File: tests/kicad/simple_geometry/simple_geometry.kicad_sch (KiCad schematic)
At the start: 2 parts

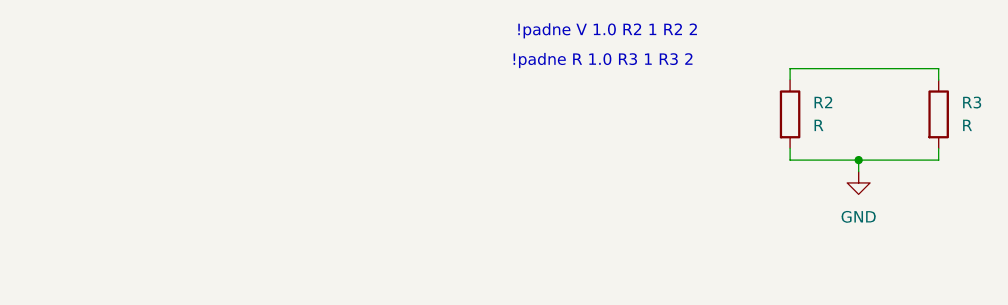
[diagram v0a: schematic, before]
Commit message: kicad: Implement basic eeschema directive parsing
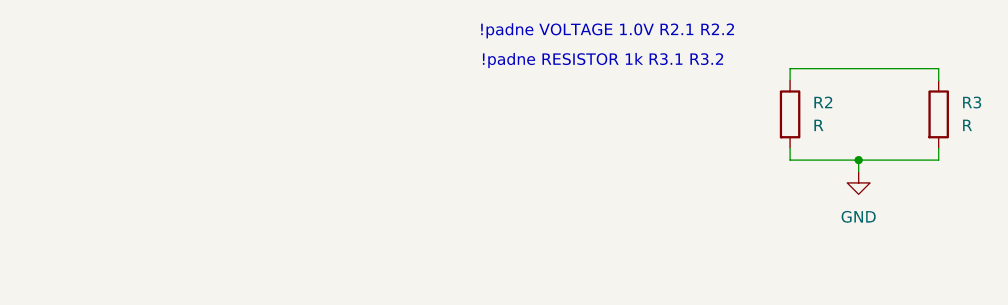
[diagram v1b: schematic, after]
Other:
- note added: "!padne RESISTOR 1k R3.1 R3.2"
- note added: "!padne VOLTAGE 1.0V R2.1 R2.2"
- note removed: "!padne R 1.0 R3 1 R3 2"
- note removed: "!padne V 1.0 R2 1 R2 2"
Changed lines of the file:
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@@
 		)
 	)
-	(text "!padne V 1.0 R2 1 R2 2"
+	(text "!padne VOLTAGE 1.0V R2.1 R2.2"
 		(exclude_from_sim no)
 		(at 119.38 96.266 0)
@@
 		)
 	)
-	(text "!padne R 1.0 R3 1 R3 2"
+	(text "!padne RESISTOR 1k R3.1 R3.2"
 		(exclude_from_sim no)
 		(at 118.872 99.568 0)

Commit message: refactor: Unify Lumped "type"
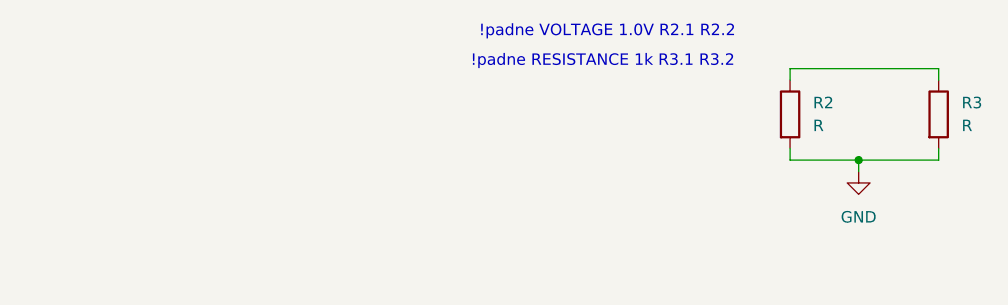
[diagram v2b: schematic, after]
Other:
- note added: "!padne RESISTANCE 1k R3.1 R3.2"
- note removed: "!padne RESISTOR 1k R3.1 R3.2"
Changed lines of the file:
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@@
 		)
 	)
-	(text "!padne RESISTOR 1k R3.1 R3.2"
+	(text "!padne RESISTANCE 1k R3.1 R3.2"
 		(exclude_from_sim no)
 		(at 118.872 99.568 0)

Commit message: feat: Use layer-specific resistivity from directives in KiCad projects
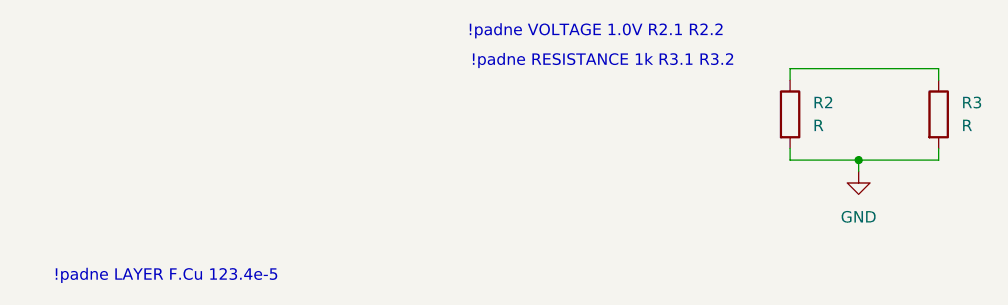
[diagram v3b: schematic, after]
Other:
- note added: "!padne LAYER F.Cu 123.4e-5"
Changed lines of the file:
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@@
 	(text "!padne VOLTAGE 1.0V R2.1 R2.2"
 		(exclude_from_sim no)
-		(at 119.38 96.266 0)
+		(at 118.11 96.266 0)
 		(effects
 			(font
@@
 		(effects
 			(font
+				(size 1.27 1.27)
+			)
+		)
+	)
+	(text "!padne LAYER F.Cu 123.4e-5"
+		(exclude_from_sim no)
+		(at 70.358 123.444 0)
+		(effects
+			(font

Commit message: refactor: resistivity -> conductance
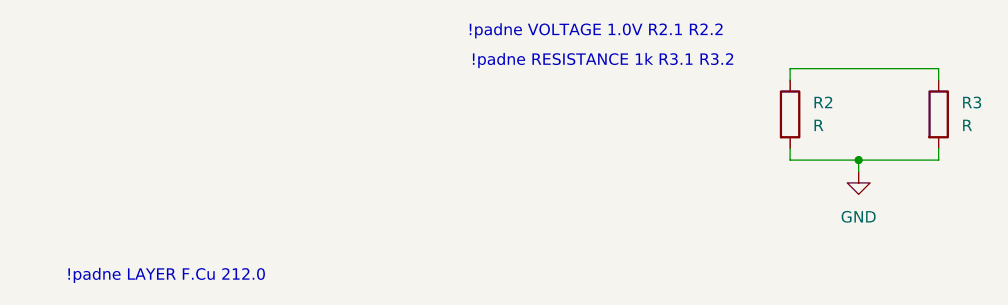
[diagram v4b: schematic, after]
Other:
- note added: "!padne LAYER F.Cu 212.0"
- note removed: "!padne LAYER F.Cu 123.4e-5"
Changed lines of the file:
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@@
 		)
 	)
-	(text "!padne LAYER F.Cu 123.4e-5"
+	(text "!padne LAYER F.Cu 212.0"
 		(exclude_from_sim no)
 		(at 70.358 123.444 0)

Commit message: test: 1k -> 0.1 resistor in simple_geometry
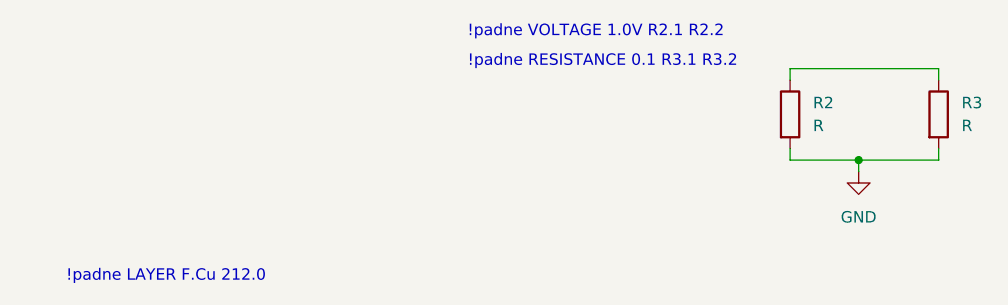
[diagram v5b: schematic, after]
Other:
- note added: "!padne RESISTANCE 0.1 R3.1 R3.2"
- note removed: "!padne RESISTANCE 1k R3.1 R3.2"
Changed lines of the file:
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@@
 		)
 	)
-	(text "!padne RESISTANCE 1k R3.1 R3.2"
+	(text "!padne RESISTANCE 0.1 R3.1 R3.2"
 		(exclude_from_sim no)
 		(at 118.872 99.568 0)

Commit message: feat: Rudimentary stackup spec support
Still veeeeeery TBD
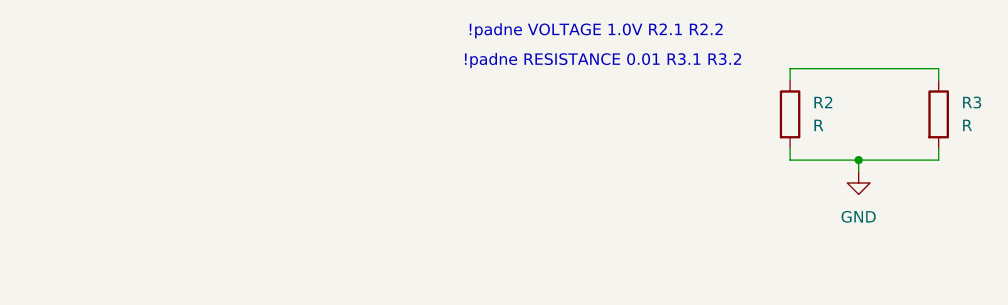
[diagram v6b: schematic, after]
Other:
- note added: "!padne RESISTANCE 0.01 R3.1 R3.2"
- note removed: "!padne LAYER F.Cu 212.0"
- note removed: "!padne RESISTANCE 0.1 R3.1 R3.2"
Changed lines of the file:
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@@
 		)
 	)
-	(text "!padne RESISTANCE 0.1 R3.1 R3.2"
+	(text "!padne RESISTANCE 0.01 R3.1 R3.2"
 		(exclude_from_sim no)
 		(at 118.872 99.568 0)
 		(effects
 			(font
-				(size 1.27 1.27)
-			)
-		)
-	)
-	(text "!padne LAYER F.Cu 212.0"
-		(exclude_from_sim no)
-		(at 70.358 123.444 0)
-		(effects
-			(font

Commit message: feat: Richer directive syntax
This commit adds support for named directive parameters. No more
guessing which parameter is the positive terminal positive and which is the
negative terminal!
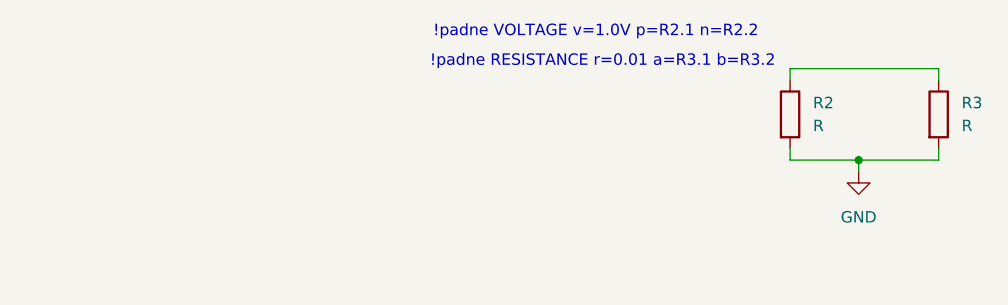
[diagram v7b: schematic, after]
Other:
- note added: "!padne RESISTANCE r=0.01 a=R3.1 b=R3.2"
- note added: "!padne VOLTAGE v=1.0V p=R2.1 n=R2.2"
- note removed: "!padne RESISTANCE 0.01 R3.1 R3.2"
- note removed: "!padne VOLTAGE 1.0V R2.1 R2.2"
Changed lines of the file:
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@@
 		)
 	)
-	(text "!padne VOLTAGE 1.0V R2.1 R2.2"
+	(text "!padne VOLTAGE v=1.0V p=R2.1 n=R2.2"
 		(exclude_from_sim no)
 		(at 118.11 96.266 0)
@@
 		)
 	)
-	(text "!padne RESISTANCE 0.01 R3.1 R3.2"
+	(text "!padne RESISTANCE r=0.01 a=R3.1 b=R3.2"
 		(exclude_from_sim no)
 		(at 118.872 99.568 0)
